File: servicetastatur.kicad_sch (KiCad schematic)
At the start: 61 parts, among them J2 Conn_02x08_Odd_Even_MountingP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, J3 Automat, SW1 OK, SW2 →, SW3 F3, SW4 F4, SW5 ←, SW6 F1, SW7 ↑, SW8 ↓, SW9 F2, U1 DIP-40 Socket, U11 PLCC-44_THT-Socket, U12 74HC573, U13 74HC165, U15 24CS16, U16 74HC238, U19 74HC4094, U2 74HC00, U20 74HC4094, U3 DIP-28 Socket, Y1 11.059, Y2 11.059

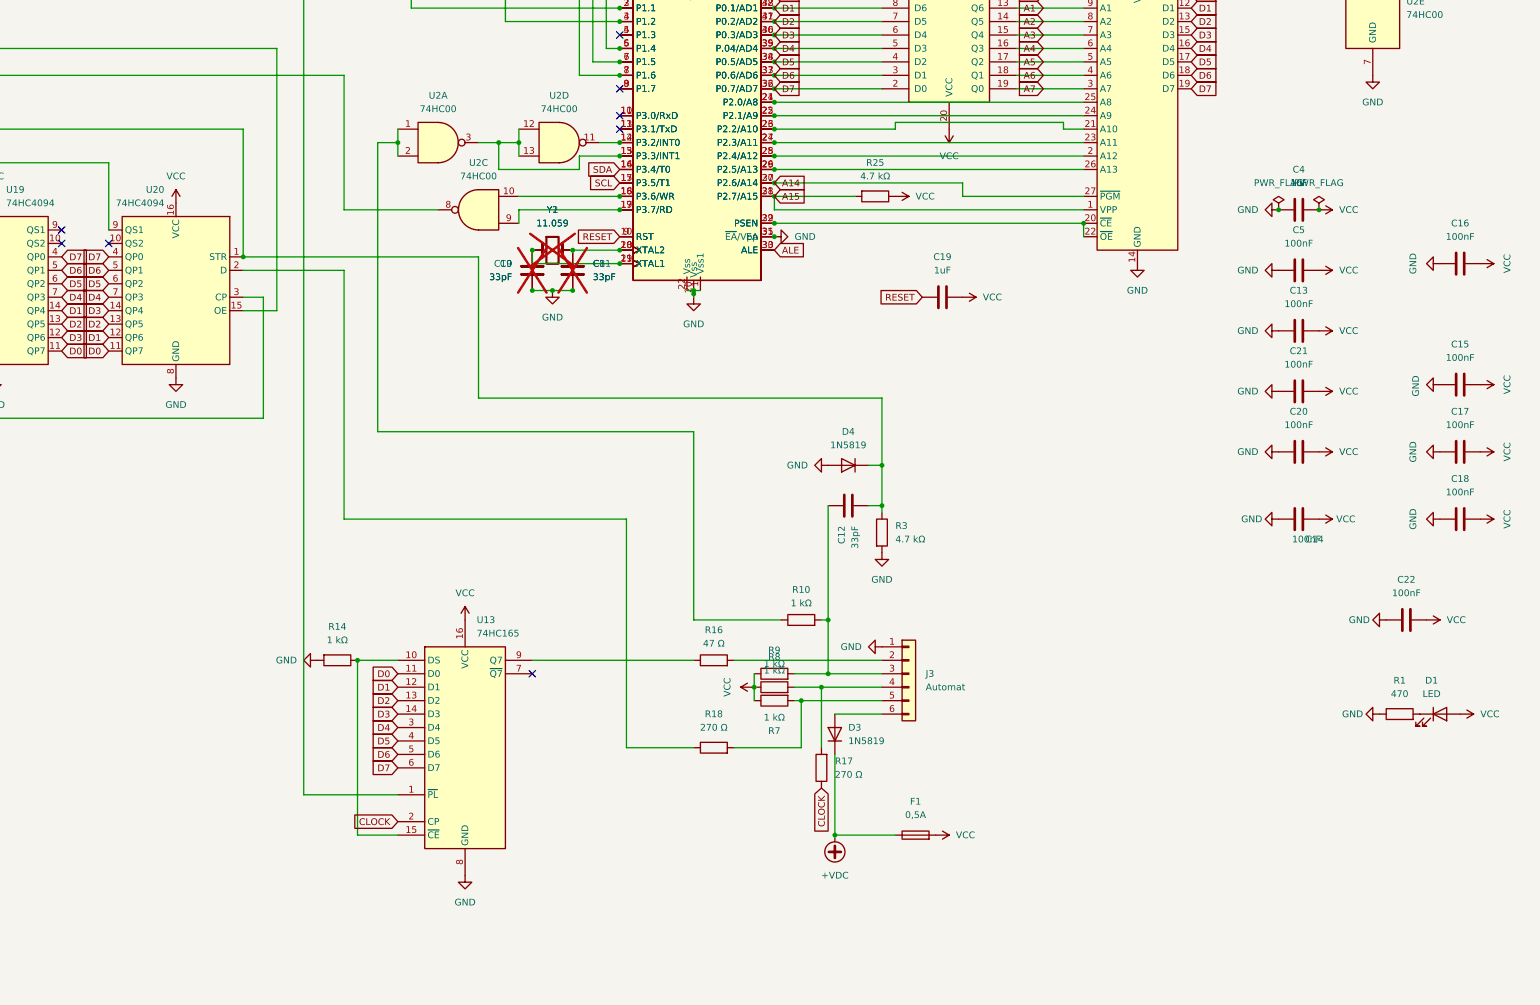
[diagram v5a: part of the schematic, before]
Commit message: reset chip
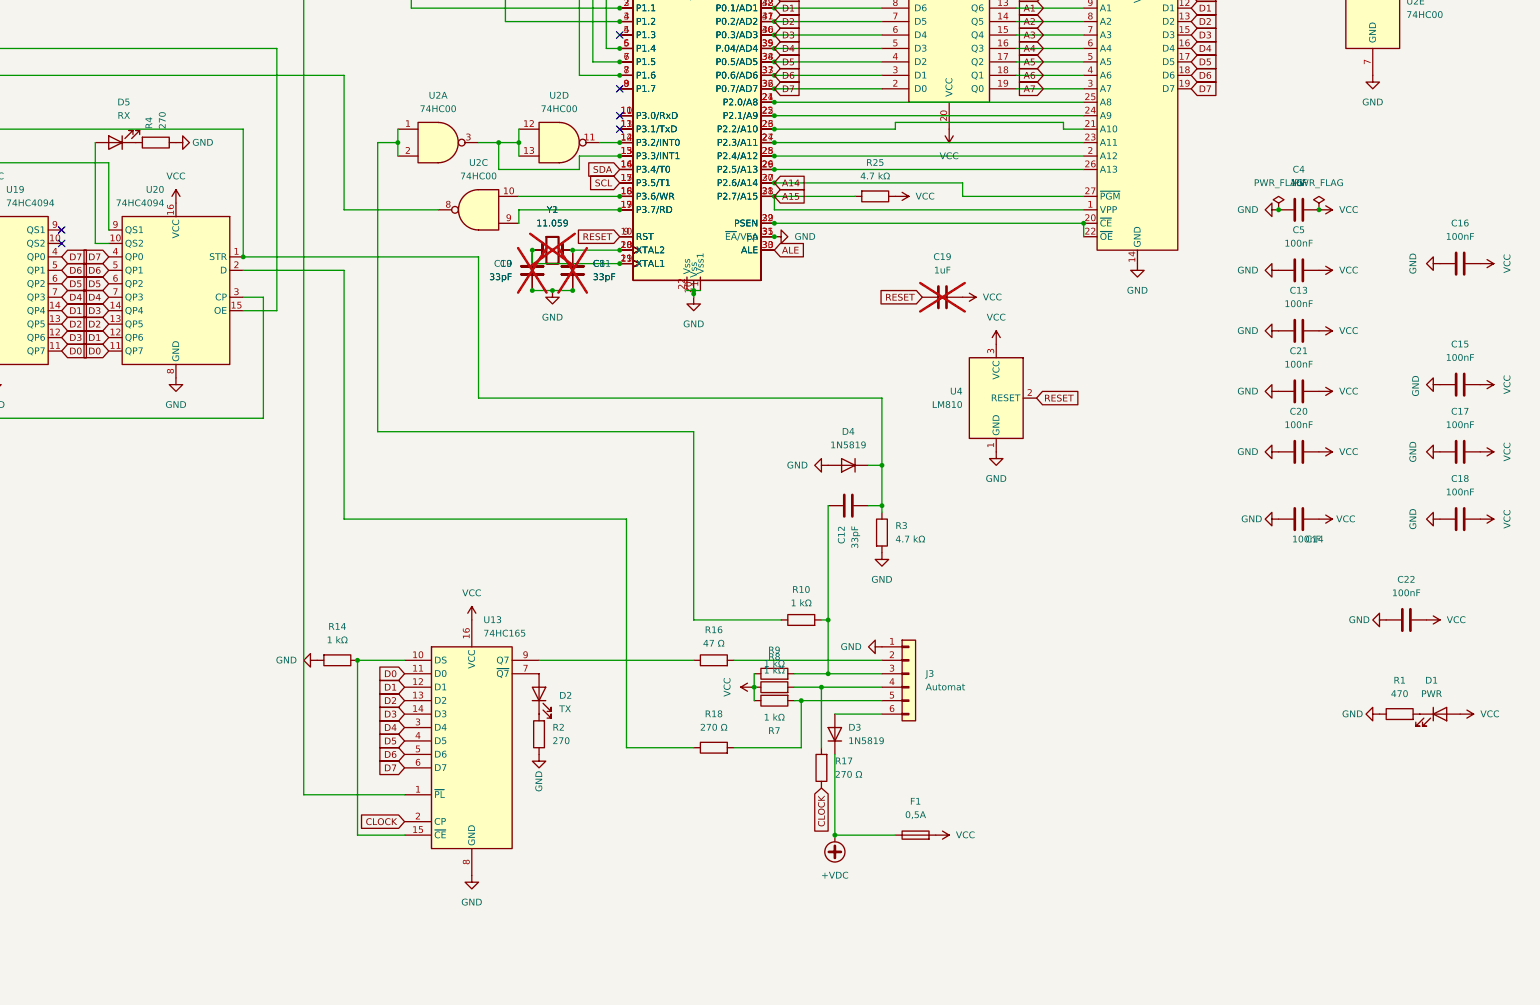
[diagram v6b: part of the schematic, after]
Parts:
- added D2: TX, LED_SMD:LED_1206_3216Metric, symbol Device:LED
- added D5: RX, LED_SMD:LED_1206_3216Metric, symbol Device:LED
- added R2, R4: 270, Resistor_SMD:R_1206_3216Metric, symbol Device:R
- added U4: LM810, Package_TO_SOT_SMD:SOT-23, symbol Power_Supervisor:LM810
- C10, C11, C12, C13, C14, C15, C16, C17, C18, C20, C21, C22, C4, C5, C8, C9: footprint Capacitor_SMD:C_0603_1608Metric -> Capacitor_SMD:C_1206_3216Metric
- C19: footprint Capacitor_SMD:C_0603_1608Metric -> Capacitor_SMD:C_1206_3216Metric; now not fitted
- D1: value LED -> PWR; footprint LED_SMD:LED_0603_1608Metric -> LED_SMD:LED_1206_3216Metric
- H1, H2: footprint MountingHole:MountingHole_3.7mm_Pad -> MountingHole:MountingHole_3.5mm_Pad
- R1, R10, R14, R16, R17, R18, R25, R3, R7, R8, R9: footprint Resistor_SMD:R_0603_1608Metric -> Resistor_SMD:R_1206_3216Metric
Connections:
- net GND: now also R2.1, R4.1, U4.1 (GND)
- net RESET: now also U4.2 (RESET)
- net VCC: now also U4.3 (VCC)
- net at U13.7 (~{Q7}): now also D2.2 (A)
- net at U20.10 (QS2): now also D5.2 (A)
- new net: D5.1 (K), R4.2
- new net: D2.1 (K), R2.2
- no-connect marks 12 -> 10
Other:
- moved on the sheet: U13

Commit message: Update servicetastatur.kicad_sch
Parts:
- J2: value Conn_02x08_Odd_Even_MountingPin -> Display
- Y1, Y2: value 11.059 -> 11.0592
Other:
- moved on the sheet: C1, C10, C11, C12, C13, C14, C15, C16, C17, C18, C19, C2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

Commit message: pin names
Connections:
- net GND: now also J3.6 (Pin_6); no longer J3.1 (Pin_1)
- net ClockIn: now reaches R17.2, R8.2
- net ClockIn: now also J3.3 (Pin_3); no longer J3.4 (Pin_4)
- net InST: now reaches R18.2, R7.2
- net InST: now also J3.2 (Pin_2); no longer J3.5 (Pin_5)
- net Enable: now reaches C12.2, R10.2, R9.2
- net Enable: now also J3.4 (Pin_4); no longer J3.3 (Pin_3)
- net OutST: now reaches R16.2
- net OutST: now also J3.5 (Pin_5); no longer J3.2 (Pin_2)
- net VBUS: now reaches D3.2 (A)
- net VBUS: now also J3.1 (Pin_1); no longer J3.6 (Pin_6)
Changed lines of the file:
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@@
 	)
 	(junction
+		(at 252.73 234.95)
+		(diameter 0)
+		(color 0 0 0 0)
+	)
+	(junction
 		(at 193.04 127)
 		(diameter 0)
@@
 		)
 	)
+	(label "InST"
+		(at 261.62 232.41 180)
+		(effects
+			(font
+				(size 1.27 1.27)
+			)
+			(justify right bottom)
+		)
+	)
+	(label "OutST"
+		(at 261.62 224.79 180)
+		(effects
+			(font
+				(size 1.27 1.27)
+			)
+			(justify right bottom)
+		)
+	)
+	(label "Enable"
+		(at 261.62 227.33 180)
+		(effects
+			(font
+				(size 1.27 1.27)
+			)
+			(justify right bottom)
+		)
+	)
 	(label "LCD_EN"
 		(at 30.48 228.6 180)
@@
 		)
 	)
+	(label "ClockIn"
+		(at 261.62 229.87 180)
+		(effects
+			(font
+				(size 1.27 1.27)
+			)
+			(justify right bottom)
+		)
+	)
 	(global_label "A14"
 		(shape input)
@@
 	)
 	(symbol
+		(lib_id "power:VBUS")
+		(at 252.73 234.95 90)
+		(unit 1)
+		(exclude_from_sim no)
+		(in_bom yes)
+		(on_board yes)
+		(dnp no)
+		(fields_autoplaced yes)
+		(property "Reference" "#PWR013"
+			(at 256.54 234.95 0)
+			(effects
+				(font
+					(size 1.27 1.27)
+				)
+				(hide yes)
+			)
+		)
+		(property "Value" "VBUS"
+			(at 248.92 234.9499 90)
+			(effects
+				(font
+					(size 1.27 1.27)
+				)
+				(justify left)
+			)
+		)
+		(property "Footprint" ""
+			(at 252.73 234.95 0)
+			(effects
+				(font
+					(size 1.27 1.27)
+				)
+				(hide yes)
+			)
+		)
+		(property "Datasheet" ""
+			(at 252.73 234.95 0)
+			(effects
+				(font
+					(size 1.27 1.27)
+				)
+				(hide yes)
+			)
+		)
+		(property "Description" "Power symbol creates a global label with name \"VBUS\""
+			(at 252.73 234.95 0)
+			(effects
+				(font
+					(size 1.27 1.27)
+				)
+				(hide yes)
+			)
+		)
+		(pin "1"
+		)
+		(instances
+			(project ""
+				(path "/f1547e98-e012-47b0-8f5e-c4ff3a098fc5"
+					(reference "#PWR013")
+					(unit 1)
+				)
+			)
+		)
+	)
+	(symbol
 		(lib_id "Device:R")
 		(at 241.3 229.87 90)
@@
 	(symbol
 		(lib_id "Connector_Generic:Conn_01x06")
-		(at 266.7 227.33 0)
+		(at 266.7 229.87 0)
+		(mirror x)
 		(unit 1)
 		(exclude_from_sim no)
@@
 		(on_board yes)
 		(dnp no)
-		(fields_autoplaced yes)
 		(property "Reference" "J3"
-			(at 269.875 227.3299 0)
+			(at 266.7 215.9 0)
 			(effects
 				(font
 					(size 1.27 1.27)
 				)
-				(justify left)
 			)
 		)
 		(property "Value" "Automat"
-			(at 269.875 229.8699 0)
+			(at 266.7 218.44 0)
 			(effects
 				(font
 					(size 1.27 1.27)
 				)
-				(justify left)
 			)
 		)
 		(property "Footprint" "ConnPad:Conn01x06"
-			(at 266.7 227.33 0)
+			(at 266.7 229.87 0)
 			(effects
 				(font
@@
 		)
 		(property "Datasheet" "~"
-			(at 266.7 227.33 0)
+			(at 266.7 229.87 0)
 			(effects
 				(font
@@
 		)
 		(property "Description" "Generic connector, single row, 01x06, script generated (kicad-library-utils/schlib/autogen/connector/)"
-			(at 266.7 227.33 0)
+			(at 266.7 229.87 0)
 			(effects
 				(font
